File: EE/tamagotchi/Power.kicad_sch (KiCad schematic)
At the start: 6 parts, among them J4 Conn_01x02, P1 USB_C_Plug_USB2.0

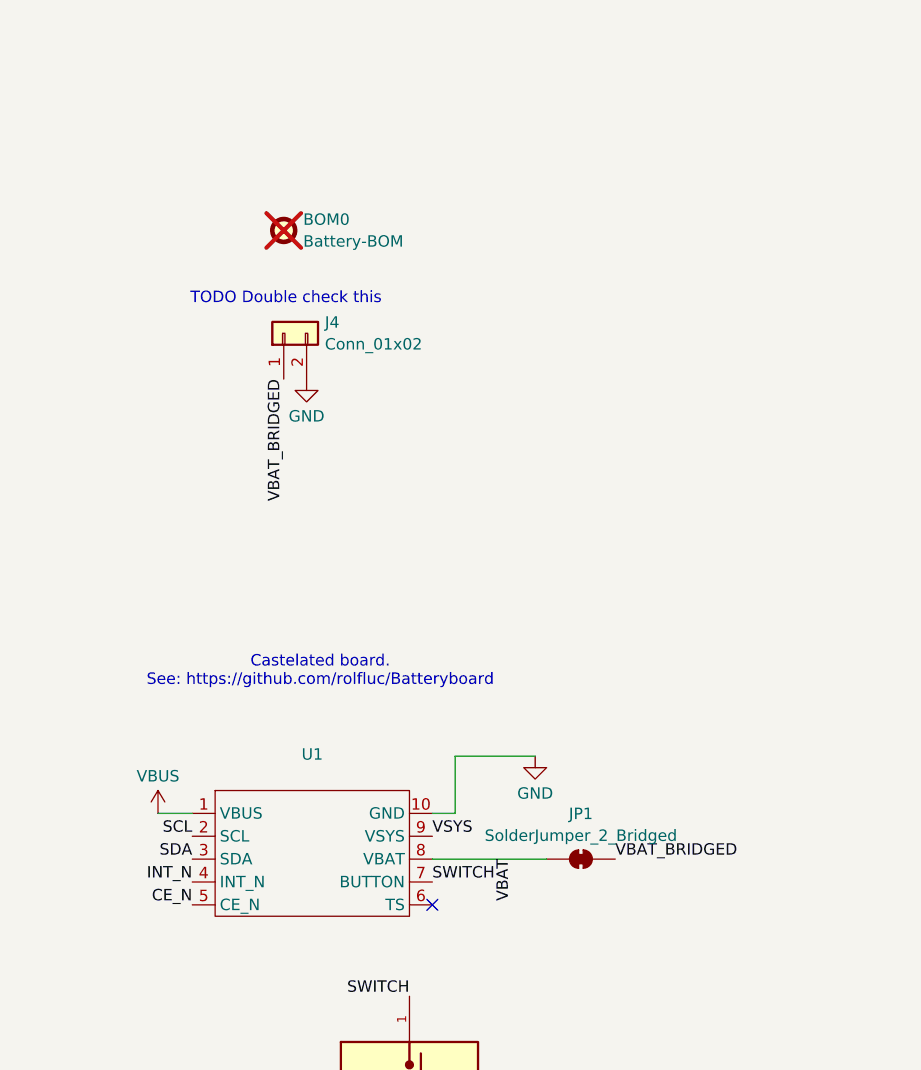
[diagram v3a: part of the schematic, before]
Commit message: Footprints and mechanical parts assigned
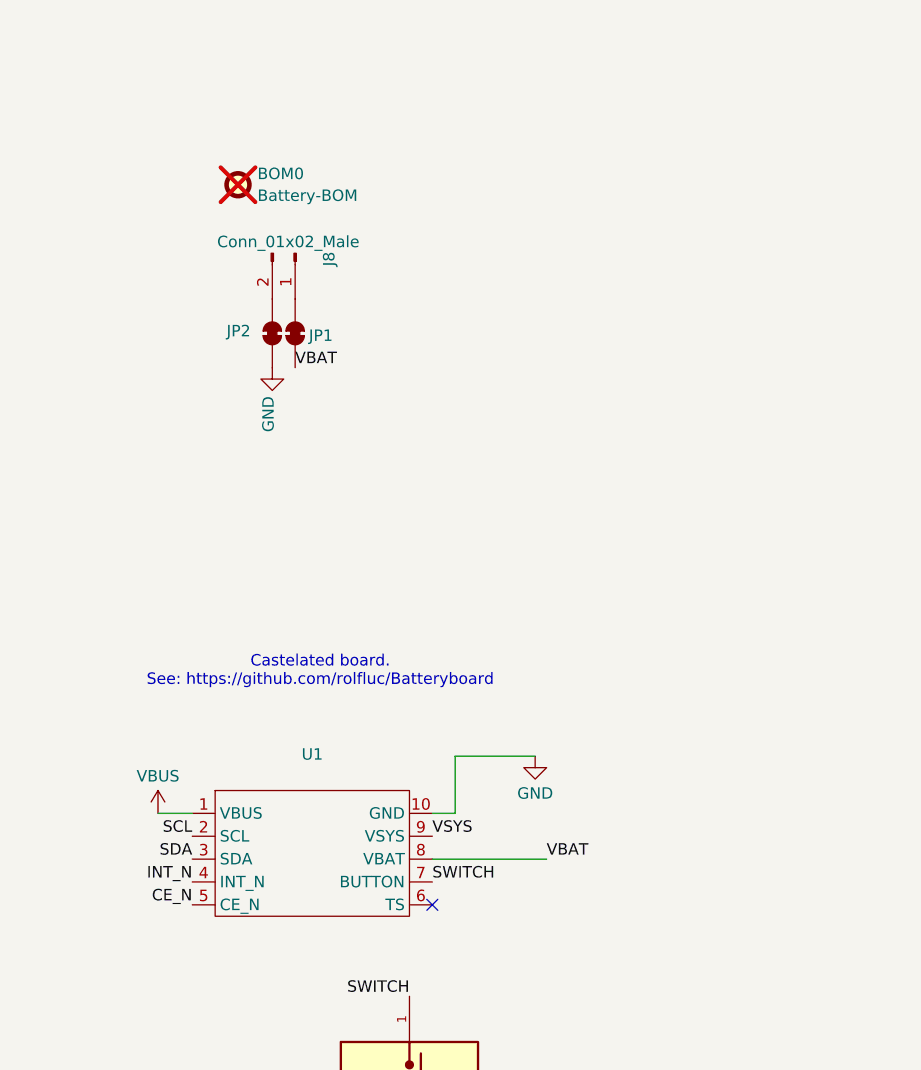
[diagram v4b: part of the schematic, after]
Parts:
- removed J4: Conn_01x02, symbol Connector_Generic:Conn_01x02
- added J8: Conn_01x02_Male, Connector_JST:JST_PH_B2B-PH-K_1x02_P2.00mm_Vertical, symbol Connector:Conn_01x02_Male
- added JP2: SolderJumper_2_Bridged, Jumper:SolderJumper-2_P1.3mm_Bridged2Bar_RoundedPad1.0x1.5mm, symbol Jumper:SolderJumper_2_Bridged
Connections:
- net GND: now also JP2.1 (A)
- net VBAT_BRIDGED: no longer names the net of JP1.1 (A)
- net VBAT_BRIDGED: now also J8.1 (Pin_1)
- new net: J8.2 (Pin_2), JP2.2 (B)
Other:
- note removed: "TODO Double check this"
- moved on the sheet: BOM0, JP1

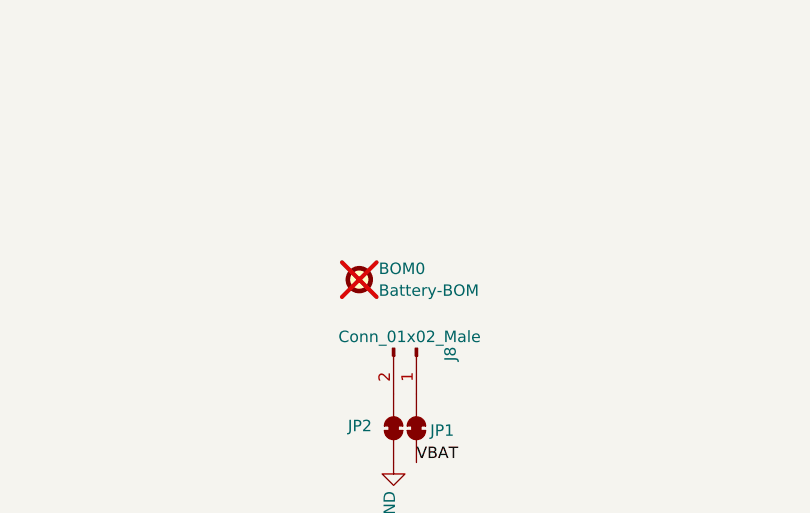
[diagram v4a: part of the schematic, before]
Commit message: Adding some new requirements for pressure / air flow
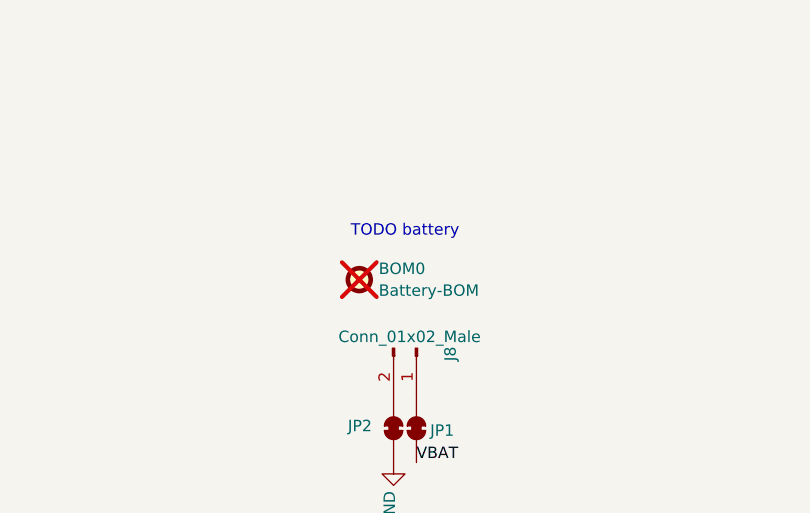
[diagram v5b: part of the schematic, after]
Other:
- note added: "TODO battery"
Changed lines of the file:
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@@
 	(generator_version "9.0")
 	(paper "A4")
+	(text "TODO battery"
+		(exclude_from_sim no)
+		(at 146.05 36.576 0)
+		(effects
+			(font
+				(size 1.27 1.27)
+			)
+		)
+	)
 	(text "Castelated board.\nSee: https://github.com/rolfluc/Batteryboard"
 		(exclude_from_sim no)

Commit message: Added pressure sensor. Re laid out board
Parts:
- J8: footprint Connector_JST:JST_PH_B2B-PH-K_1x02_P2.00mm_Vertical -> Connector_JST:JST_PH_S2B-PH-SM4-TB_1x02-1MP_P2.00mm_Horizontal
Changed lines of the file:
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@@
 			)
 		)
-		(property "Footprint" "Connector_JST:JST_PH_B2B-PH-K_1x02_P2.00mm_Vertical"
+		(property "Footprint" "Connector_JST:JST_PH_S2B-PH-SM4-TB_1x02-1MP_P2.00mm_Horizontal"
 			(at 147.32 49.53 0)
 			(effects
